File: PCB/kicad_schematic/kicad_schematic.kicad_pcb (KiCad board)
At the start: 2 copper layers, 69.5 x 97 mm, 25 parts, among them J1 Conn_01x08_Pin, SW1 SW_Push, SW2 SW_Push, SW3 SW_Push, SW4 SW_Push, SW5 SW_Push, SW6 SW_Push, SW7 SW_Push, SW8 SW_Push, SW9 SW_Push, U1 XIAO-ESP32-C3-SMD

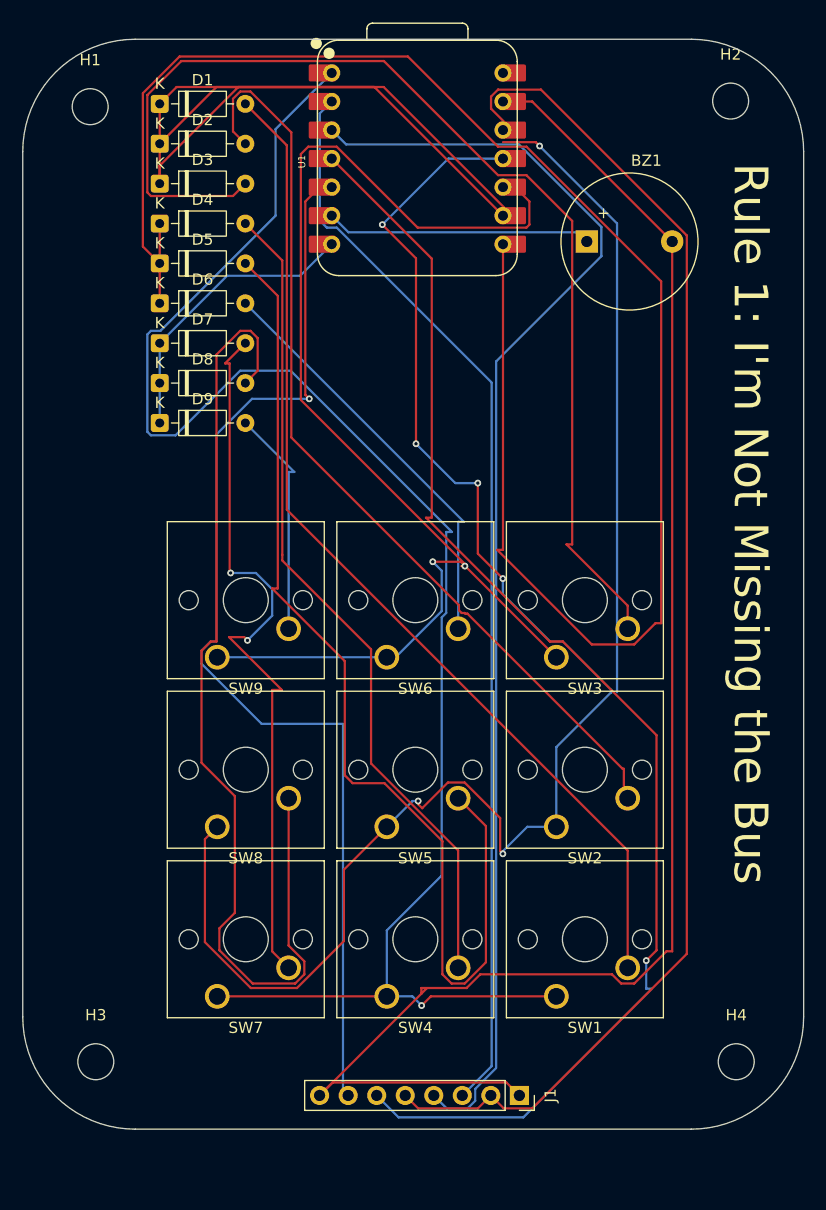
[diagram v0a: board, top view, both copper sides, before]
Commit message: respace key matrix to 19.05mm and reroute
the 3x3 matrix was on 15.09mm centres. an mx switch is 15.6mm across the
plate flange and a 1u dsa cap is 18.4mm, so neither the switches nor the
caps could physically be fitted. moved to standard 19.05mm pitch.

- switch centres x 77.70/96.75/115.80, y 52.00/71.05/90.10
- one diode per switch, in the gap directly below it, instead of a column
  of nine at the board edge
- H3 and H4 moved outward in x to clear the wider key block
- U1 and J1 flipped to B.Cu per the blare guide, buzzer left on F.Cu
- fully rerouted, 461 tracks and 14 vias, drc clean with nothing unrouted
- fixes 17 co-located drill holes and 6 dangling tracks/vias in the old
  routing

board outline, netlist and schematic are unchanged.

also adds the drill file, which was missing, and renames the stray
PCB/.step to PCB/board.step.
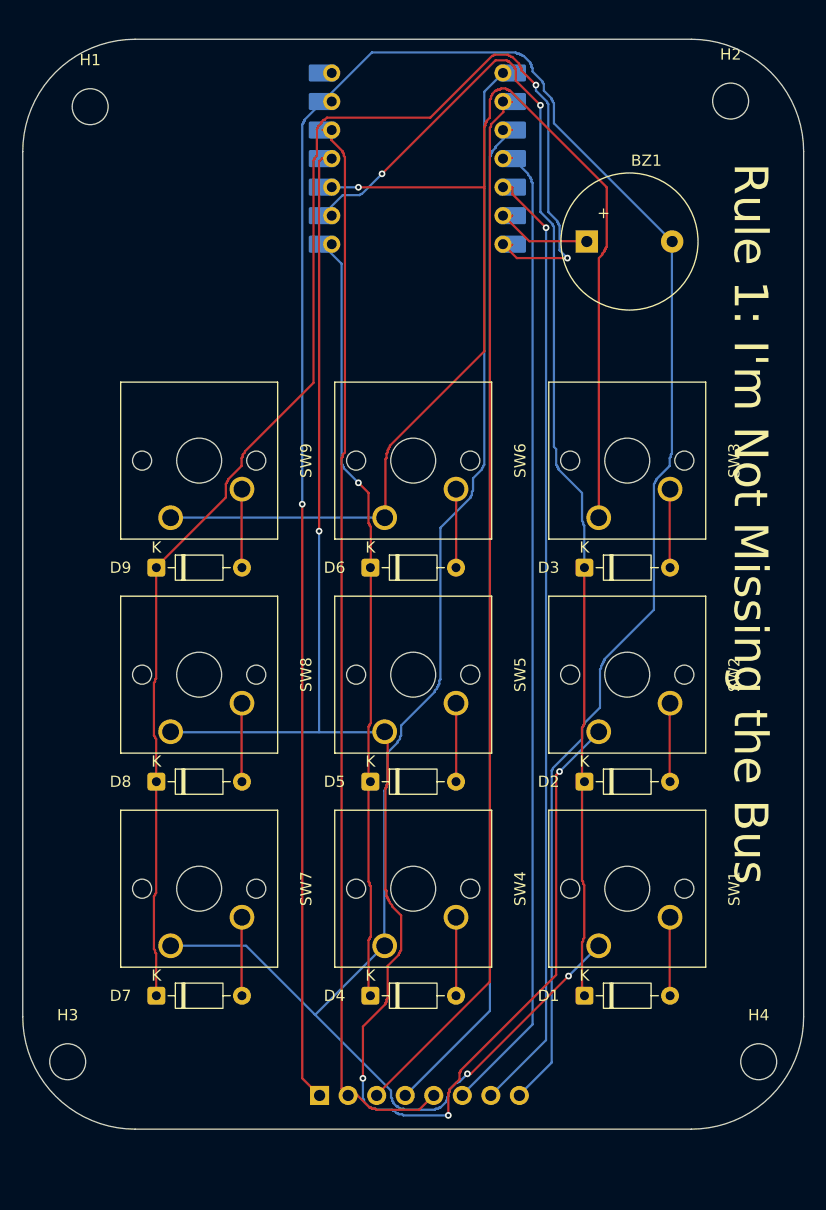
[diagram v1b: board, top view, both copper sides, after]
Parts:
- J1, U1: moved to B.Cu
- moved D1 87.9 mm to (112.0, 99.6)
- moved D4 71.2 mm to (92.9, 99.6)
- moved D2 68.2 mm to (112.0, 80.6)
- moved D7 58.1 mm to (73.9, 99.6)
- moved D3 51.0 mm to (112.0, 61.5)
- moved D5 49.8 mm to (92.9, 80.6)
- moved D8 35.5 mm to (73.9, 80.6)
- moved D6 30.1 mm to (92.9, 61.5)
- moved J1 17.8 mm to (88.4, 108.5)
- moved SW9 13.1 mm to (75.2, 57.1)
- moved SW3 13.0 mm to (113.3, 57.1)
- moved D9 12.9 mm to (73.9, 61.5)
- moved SW6 12.4 mm to (94.2, 57.1)
- moved SW8 9.42 mm to (75.2, 76.1)
- moved SW2 9.26 mm to (113.3, 76.1)
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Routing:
- net Net-(D3-A): track 156.9 -> 6.90 mm, vias 1 -> 0
- net Net-(D7-K): track 26.1 -> 130.5 mm, vias 0 -> 2
- net Net-(D5-A): track 93.5 -> 7.00 mm
- net Net-(D4-K): track 155.6 -> 69.8 mm, vias 0 -> 1
- net Net-(D1-A): track 91.0 -> 7.00 mm
- net Net-(D8-A): track 90.3 -> 7.00 mm
- net Net-(D2-A): track 83.8 -> 7.00 mm
- net GND: track 139.7 -> 213.8 mm
- net Net-(D4-A): track 74.1 -> 7.00 mm
- net Net-(D7-A): track 66.0 -> 7.00 mm, vias 2 -> 0
- net Net-(J1-Pin_6): track 118.2 -> 87.6 mm, vias 1 -> 0
- net Net-(D6-A): track 37.5 -> 6.90 mm
- net +3.3V: track 122.9 -> 96.2 mm, vias 1 -> 0
- net Net-(J1-Pin_4): track 114.4 -> 90.3 mm, vias 1 -> 0
- net Net-(BZ1-+): track 23.7 -> 8.92 mm, vias 1 -> 0
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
